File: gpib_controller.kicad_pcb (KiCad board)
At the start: 2 copper layers, 61.5 x 44 mm, 23 parts, among them J1 112-024-113R001, J2 FTSH-105-01-L-DV-K, J3 RJHSE5380, U1 SN74LVC8T245PWR, U2 SN74LVC07APWR, U3 STM32H533RETx, U4 PTS645SH43SMTR92 LFS, U5 THVD1451D, U6 SN74LVC1G07DCKR, Y1 MU00525-32.768K, Y2 CS10820-24M

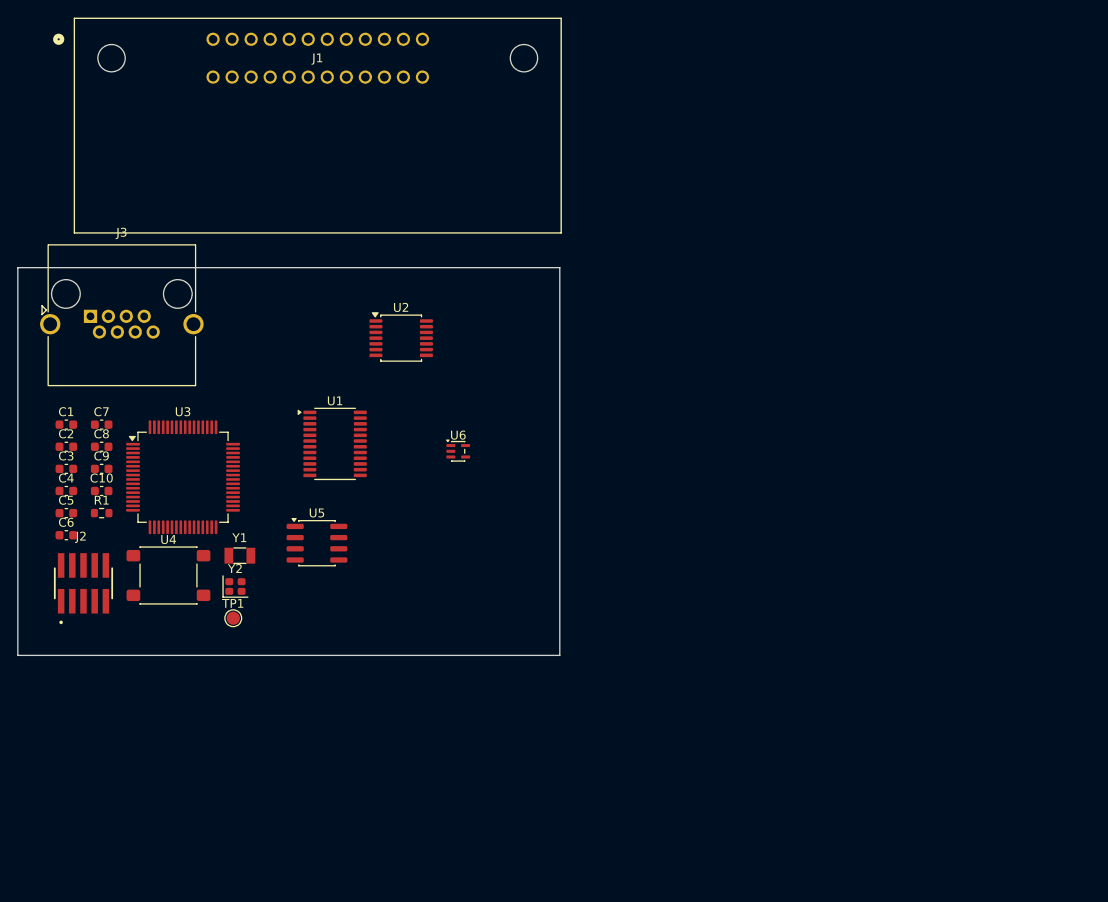
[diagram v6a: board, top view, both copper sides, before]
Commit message: Add power supply and USB protection
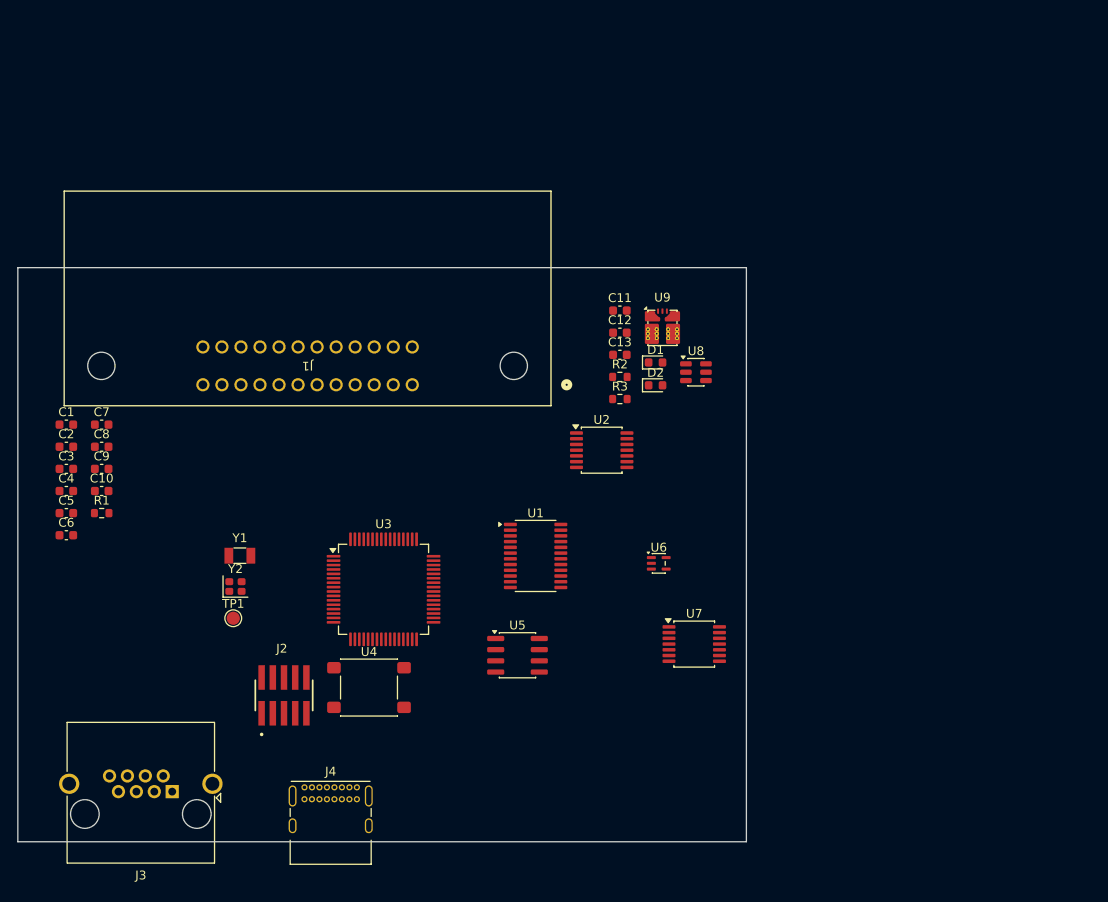
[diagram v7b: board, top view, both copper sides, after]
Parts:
- added C11: 100nF, Capacitor_SMD:C_0603_1608Metric, F.Cu at (201.8, 72.9)
- added C12: 10 µF, Capacitor_SMD:C_0603_1608Metric, F.Cu at (201.8, 75.4)
- added C13: 100nF, Capacitor_SMD:C_0603_1608Metric, F.Cu at (201.8, 77.9)
- added D1: Green, LED_SMD:LED_0603_1608Metric, F.Cu at (205.9, 78.8)
- added D2: Red, LED_SMD:LED_0603_1608Metric, F.Cu at (205.9, 81.3)
- added J4: USB4085-GF-A, Connector_USB:USB_C_Receptacle_GCT_USB4085, F.Cu at (166.0, 127.0)
- added R2: 15.8k, Resistor_SMD:R_0603_1608Metric, F.Cu at (201.8, 80.4)
- added R3: 10k, Resistor_SMD:R_0603_1608Metric, F.Cu at (201.8, 82.9)
- added U7: SN74LVC14APWR, Package_SO:TSSOP-14_4.4x5mm_P0.65mm, F.Cu at (210.3, 110.7)
- added U8: USBLC6-2SC6, Package_TO_SOT_SMD:SOT-23-6, F.Cu at (210.4, 79.9)
- added U9: TPSM861253RDXR, Package_DFN_QFN:Texas_RDX0007A_QFN-FCMOD-7-3.3x4mm-P0.5mm_4EP, F.Cu at (206.7, 74.8)
- moved J3 54.7 mm to (151.0, 127.5), turned to 180 degrees
- moved J1 45.3 mm to (178.3, 81.3), turned to 180 degrees
- moved J2 26.1 mm to (163.7, 116.5)
- moved U1 26.1 mm to (192.3, 100.7)
- moved U2 26.1 mm to (199.8, 88.7)
- moved U3 26.1 mm to (175.0, 104.5)
- moved U4 26.1 mm to (173.3, 115.7)
- moved U5 26.1 mm to (190.2, 112.0)
- moved U6 26.1 mm to (206.2, 101.6)
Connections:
- J1 pad 10: unconnected-(J1-Pin_10-Pad10) -> /Overview/Connectors/ATN
- J1 pad 11: unconnected-(J1-Pin_11-Pad11) -> /Overview/Connectors/ATN
- J1 pad 12: unconnected-(J1-Pin_12-Pad12) -> GND
- J1 pad 17: unconnected-(J1-Pin_17-Pad17) -> /Overview/Connectors/ATN
- J1 pad 5: unconnected-(J1-Pin_5-Pad5) -> /Overview/Connectors/ATN
- J1 pad 6: unconnected-(J1-Pin_6-Pad6) -> /Overview/Connectors/ATN
- J1 pad 7: unconnected-(J1-Pin_7-Pad7) -> /Overview/Connectors/ATN
- J1 pad 8: unconnected-(J1-Pin_8-Pad8) -> /Overview/Connectors/ATN
- J1 pad 9: unconnected-(J1-Pin_9-Pad9) -> /Overview/Connectors/ATN
- U2 pad 10: unconnected-(U2-5Y-Pad10) -> /Overview/Connectors/ATN
- U2 pad 12: unconnected-(U2-6Y-Pad12) -> /Overview/Connectors/ATN
- U2 pad 2: unconnected-(U2-1Y-Pad2) -> /Overview/Connectors/ATN
- U2 pad 4: unconnected-(U2-2Y-Pad4) -> /Overview/Connectors/ATN
- U2 pad 6: unconnected-(U2-3Y-Pad6) -> /Overview/Connectors/ATN
- U2 pad 8: unconnected-(U2-4Y-Pad8) -> /Overview/Connectors/ATN
- U3 pad 21: /Overview/Microcontroller/DAV_SENSE -> /Overview/GPIB Transceiver/DAV_SENSE
- U3 pad 22: /Overview/Microcontroller/NRFD_SENSE -> /Overview/GPIB Transceiver/NRFD_SENSE
- U3 pad 23: /Overview/Microcontroller/NDAC_SENSE -> /Overview/GPIB Transceiver/NDAC_SENSE
- U3 pad 29: /Overview/Microcontroller/EOI_SENSE -> /Overview/GPIB Transceiver/EOI_SENSE
- U3 pad 33: /Overview/Microcontroller/SRQ_SENSE -> /Overview/GPIB Transceiver/SRQ_SENSE
- U3 pad 44: /Overview/Microcontroller/USB_DM -> /Overview/Microcontroller/iUSB_DM
- U3 pad 45: /Overview/Microcontroller/USB_DP -> /Overview/Microcontroller/iUSB_DP
- U6 pad 4: unconnected-(U6-Y-Pad4) -> /Overview/Connectors/ATN
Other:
- board size 61.5 x 44 mm -> 82.7 x 65.1 mm

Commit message: Start work on PCB
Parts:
- added C13: 2.2 µF, Capacitor_SMD:C_0603_1608Metric, F.Cu at (202.0, 127.8)
- added C14: 22 µF, Capacitor_SMD:C_0603_1608Metric, F.Cu at (196.0, 120.3)
- added C15: 10000 pF, Capacitor_SMD:C_0603_1608Metric, F.Cu at (196.0, 122.8)
- added C16: 2.2 µF, Capacitor_SMD:C_0603_1608Metric, F.Cu at (202.0, 130.3)
- added R4: 150, Resistor_SMD:R_0603_1608Metric, F.Cu at (196.0, 125.3)
- added R5: 68, Resistor_SMD:R_0603_1608Metric, F.Cu at (196.0, 127.8)
- added R6: 5.1k, Resistor_SMD:R_0603_1608Metric, F.Cu at (208.0, 127.8)
- added R7: 5.1k, Resistor_SMD:R_0603_1608Metric, F.Cu at (208.0, 130.3)
- added R8: 2.2k, Resistor_SMD:R_Array_Convex_8x0602, F.Cu at (202.1, 121.8)
- moved C2 39.9 mm to (178.0, 96.7), turned to -90 degrees
- moved C1 28.3 mm to (166.5, 92.5)
- moved TP1 12.6 mm to (154.8, 95.6)
- moved Y1 12.6 mm to (155.5, 88.5)
- moved Y2 12.6 mm to (155.0, 92.0)
- moved U3 6.42 mm to (170.2, 100.2)
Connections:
- D1 pad 1: unconnected-(D1-K-Pad1) -> Net-(D1-K)
- D2 pad 1: unconnected-(D2-K-Pad1) -> Net-(D2-K)
- J1 pad 13: unconnected-(J1-Pin_13-Pad13) -> /Overview/Connectors/DIO5
- J4 pad A5: unconnected-(J4-CC1-PadA5) -> Net-(J4-CC1)
- J4 pad B5: unconnected-(J4-CC2-PadB5) -> Net-(J4-CC2)
- U1 pad 17: unconnected-(U1-B5-Pad17) -> /Overview/Connectors/DIO5
- U1 pad 2: unconnected-(U1-DIR-Pad2) -> /Overview/GPIB Transceiver/GPIB_DIR
- U1 pad 22: unconnected-(U1-~{OE}-Pad22) -> /Overview/GPIB Transceiver/GPIB_EN
- U1 pad 7: unconnected-(U1-A5-Pad7) -> /Overview/GPIB Transceiver/iDIO5
- U3 pad 30: unconnected-(U3A-VCAP-Pad30) -> Net-(C13-Pad1)
- U3 pad 39: unconnected-(U3H-PC8-Pad39) -> /Overview/GPIB Transceiver/GPIB_EN
- U3 pad 40: unconnected-(U3H-PC9-Pad40) -> /Overview/GPIB Transceiver/GPIB_DIR
- U3 pad 62: unconnected-(U3A-VCAP-Pad62) -> Net-(C13-Pad1)
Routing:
- net /Overview/GPIB Transceiver/iDIO4: track 0.00 -> 20.6 mm
- net /Overview/GPIB Transceiver/iDIO5: track 0.00 -> 7.56 mm
- net /Overview/GPIB Transceiver/iDIO6: track 0.00 -> 6.56 mm
- net /Overview/GPIB Transceiver/iDIO1: track 0.00 -> 5.28 mm
- net /Overview/GPIB Transceiver/iDIO2: track 0.00 -> 5.18 mm
- net /Overview/GPIB Transceiver/iDIO3: track 0.00 -> 4.93 mm
